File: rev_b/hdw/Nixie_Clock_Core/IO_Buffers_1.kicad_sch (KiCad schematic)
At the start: 14 parts, among them U2801 74VHC541, U2802 74VHC541, U2803 74LVC1G97, U2804 74LVC1G97

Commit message: lots of rev B control board schematic progress
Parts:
- removed C? (x2): 0.1uF, Capacitors_SMD:C_0603, symbol Custom_Library:C_Custom
- removed R? (x2): 10K, Resistors_SMD:R_0603, symbol Custom_Library:R_Custom
- removed U2803, U2804: 74LVC1G97, Package_TO_SOT_SMD:SOT-363_SC-70-6, symbol Custom_Library:74LVC1G97_Power_BUF
- renumbered RN2801 to RN?, RN2802 to RN?, U2801 to U?, U2802 to U?
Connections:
- net +5V is gone; now on net +3.3V: C?.1, C?.1, U?.20 (VCC), U?.20 (VCC)
- net Grid_2 is gone; now on net Anode_DP: RN?.14 (R3.2), U?.4 (A2)
- net Grid_3 is gone; now on net Colon_0: RN?.13 (R4.2), U?.5 (A3)
- net Grid_4 is gone; now on net Colon_1: RN?.12 (R5.2), U?.6 (A4)
- net Grid_5 is gone; now on net Colon_2: RN?.11 (R6.2), U?.7 (A5)
- net Anode_DP: no longer RN?.9 (R8.2), U?.9 (A7)
- net Colon_0: no longer RN?.10 (R7.2), U?.8 (A6)
- net Colon_1: no longer RN?.9 (R8.2), U?.9 (A7)
- net Colon_3: now also RN?.10 (R7.2), U?.8 (A6)
- net Anode_A renamed Anode_0
- net Anode_A_DSP: no longer names the net of U?.18 (Y0)
- net Anode_B renamed Anode_1
- net Anode_B_DSP: no longer names the net of U?.17 (Y1)
- net Anode_C renamed Anode_2
- net Anode_C_DSP: no longer names the net of U?.16 (Y2)
- net Anode_D renamed Anode_3
- net Anode_DP_DSP: no longer names the net of U?.11 (Y7)
- net Anode_D_DSP: no longer names the net of U?.15 (Y3)
- net Anode_E renamed Anode_4
- net Anode_E_DSP: no longer names the net of U?.14 (Y4)
- net Anode_F renamed Anode_5
- net Anode_F_DSP: no longer names the net of U?.13 (Y5)
- net Anode_G renamed Anode_6
- net Anode_G_DSP: no longer names the net of U?.12 (Y6)
- net Colon_0_DSP: no longer names the net of U?.12 (Y6)
- net Colon_1_DSP: no longer names the net of U?.11 (Y7)
- net Grid_0 renamed Anode_8
- net Grid_0_DSP: no longer names the net of U?.18 (Y0)
- net Grid_1 renamed Anode_9
- net Grid_1_DSP: no longer names the net of U?.17 (Y1)
- net Grid_2_DSP: no longer names the net of U?.16 (Y2)
- net Grid_3_DSP: no longer names the net of U?.15 (Y3)
- net Grid_4_DSP: no longer names the net of U?.14 (Y4)
- net Grid_5_DSP: no longer names the net of U?.13 (Y5)
- new net: RN?.9 (R8.2), U?.9 (A7)
- new net Anode_7: RN?.9 (R8.2), U?.9 (A7)

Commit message: more rev b sch progress
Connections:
- net Anode_7_DSP: now reaches U?.11 (Y7)
- net Anode_6_DSP: now reaches U?.12 (Y6)
- net Anode_5_DSP: now reaches U?.13 (Y5)
- net Anode_4_DSP: now reaches U?.14 (Y4)
- net Anode_3_DSP: now reaches U?.15 (Y3)
- net Anode_2_DSP: now reaches U?.16 (Y2)
- net Anode_1_DSP: now reaches U?.17 (Y1)
- net Anode_0_DSP: now reaches U?.18 (Y0)
- net Colon_3_DSP: now reaches U?.12 (Y6)
- net Colon_2_DSP: now reaches U?.13 (Y5)
- net Colon_1_DSP: now reaches U?.14 (Y4)
- net Colon_0_DSP: now reaches U?.15 (Y3)
- net Anode_DP_DSP: now reaches U?.16 (Y2)
- net Anode_9_DSP: now reaches U?.17 (Y1)
- net Anode_8_DSP: now reaches U?.18 (Y0)
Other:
- moved on the sheet: RN?, U?

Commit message: more carrier board progress
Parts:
- removed C?: 0.1uF, Capacitors_SMD:C_0603, symbol Custom_Library:C_Custom
- removed R?: 10K, Resistors_SMD:R_0603, symbol Custom_Library:R_Custom
- removed RN?: 10k, Resistors_SMD:R_Array_Convex_8x0602, symbol Device:R_Pack08
- removed U?: 74VHC541, Package_DFN_QFN:WQFN-20-1EP_2.5x4.5mm_P0.5mm_EP1x2.9mm, symbol Custom_Library:74VHC541
- added C? (x2): 0.1uF, Capacitors_SMD:C_0603, symbol Custom_Library:C_Custom
- added R? (x2): 10K, Resistors_SMD:R_0603, symbol Custom_Library:R_Custom
- added RN? (x2): 10k, Resistors_SMD:R_Array_Convex_8x0602, symbol Device:R_Pack08
- added U? (x2): 74VHC541, Package_DFN_QFN:WQFN-20-1EP_2.5x4.5mm_P0.5mm_EP1x2.9mm, symbol Custom_Library:74VHC541
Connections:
- net +3.3V: now also C?.1, C?.1, R?.1, R?.1, U?.20 (VCC), U?.20 (VCC)
- net Colon_0: now also RN?.13 (R4.2), U?.5 (A3)
- net Colon_0_DSP: now also U?.15 (Y3)
- net Colon_1: now also RN?.12 (R5.2), U?.6 (A4)
- net Colon_1_DSP: now also U?.14 (Y4)
- net Colon_2: now also RN?.11 (R6.2), U?.7 (A5)
- net Colon_2_DSP: now also U?.13 (Y5)
- net Colon_3: now also RN?.10 (R7.2), U?.8 (A6)
- net Colon_3_DSP: now also U?.12 (Y6)
- net GND: now also C?.2, C?.2, RN?.1 (R1.1), RN?.1 (R1.1), RN?.2 (R2.1), RN?.2 (R2.1), RN?.3 (R3.1), RN?.3 (R3.1), RN?.4 (R4.1), RN?.4 (R4.1), RN?.5 (R5.1), RN?.5 (R5.1), RN?.6 (R6.1), RN?.6 (R6.1), RN?.7 (R7.1), RN?.7 (R7.1), RN?.8 (R8.1), RN?.8 (R8.1), U?.10 (GND), U?.10 (GND), U?.21 (GND), U?.21 (GND)
- net ~{IO_Level_Shift_Enable}: now also R?.2, R?.2, U?.1 (G1), U?.1 (G1), U?.19 (G2), U?.19 (G2)
- net Anode_6: no longer names the net of RN?.10 (R7.2), U?.8 (A6)
- net Anode_6_DSP: no longer names the net of U?.12 (Y6)
- net Anode_7: no longer names the net of RN?.9 (R8.2), U?.9 (A7)
- net Anode_7_DSP: no longer names the net of U?.11 (Y7)
- new net: RN?.9 (R8.2), U?.9 (A7)
- new net Cathode_0: RN?.16 (R1.2), U?.2 (A0)
- new net Cathode_0_DSP: U?.18 (Y0)
- new net Cathode_1: RN?.15 (R2.2), U?.3 (A1)
- new net Cathode_1_DSP: U?.17 (Y1)
- new net Cathode_2: RN?.14 (R3.2), U?.4 (A2)
- new net Cathode_2_DSP: U?.16 (Y2)
- new net Cathode_3: RN?.13 (R4.2), U?.5 (A3)
- new net Cathode_3_DSP: U?.15 (Y3)
- new net Cathode_4: RN?.12 (R5.2), U?.6 (A4)
- new net Cathode_4_DSP: U?.14 (Y4)
- new net Cathode_5: RN?.11 (R6.2), U?.7 (A5)
- new net Cathode_5_DSP: U?.13 (Y5)
- new net Cathode_6: RN?.10 (R7.2), U?.8 (A6)
- new net Cathode_6_DSP: U?.12 (Y6)
- new net Cathode_7: RN?.9 (R8.2), U?.9 (A7)
- new net Cathode_7_DSP: U?.11 (Y7)
- new net Cathode_8: RN?.16 (R1.2), U?.2 (A0)
- new net Cathode_8_DSP: U?.18 (Y0)
- new net Cathode_9: RN?.15 (R2.2), U?.3 (A1)
- new net Cathode_9_DSP: U?.17 (Y1)
- new net Cathode_DP: RN?.14 (R3.2), U?.4 (A2)
- new net Cathode_DP_DSP: U?.16 (Y2)
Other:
- note removed: "CONSIDER SINGLE RESISTORS INSTEAD OF RPACKS"
- moved on the sheet: C?, R?, RN?, U?

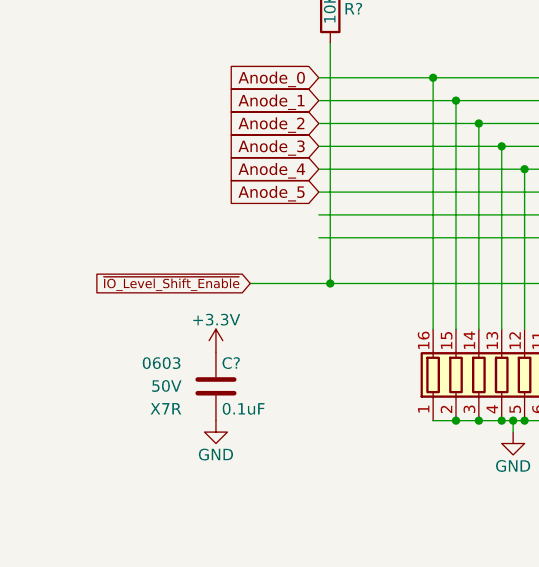
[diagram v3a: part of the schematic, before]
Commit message: more schematic progress, assigning signals to MCU"
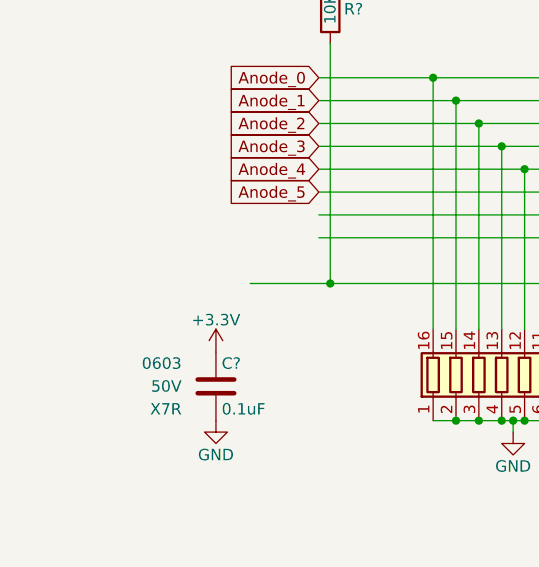
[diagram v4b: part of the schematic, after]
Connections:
- net ~{IO_Level_Shift_Enable}: no longer R?.2, U?.1 (G1), U?.19 (G2)
- new net: R?.2, U?.1 (G1), U?.19 (G2)
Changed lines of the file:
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@@
-    )
-  )
-  (global_label "~{IO_Level_Shift_Enable}" (shape input) (at 36.83 58.42 180)
-    (effects (font (size 1.016 1.016)) (justify right))
-    (property "Intersheetrefs" "${INTERSHEET_REFS}" (at 36.83 58.42 0)
-      (effects (font (size 1.27 1.27)) hide)
     )
   )

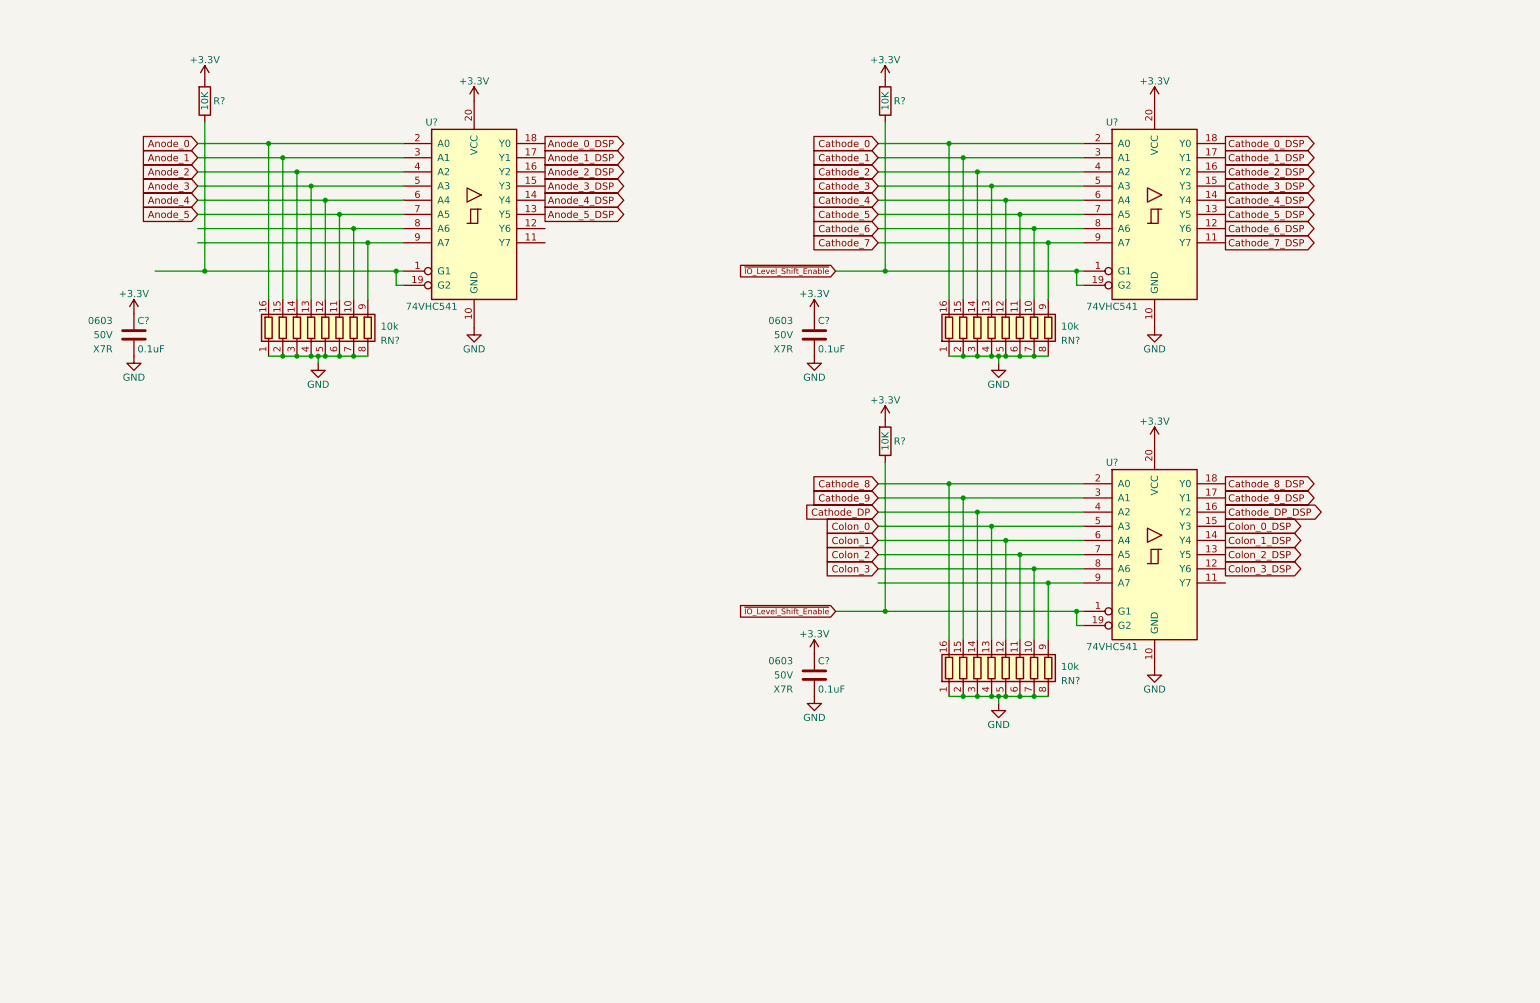
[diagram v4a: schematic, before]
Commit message: updated footprints, ran some DRC
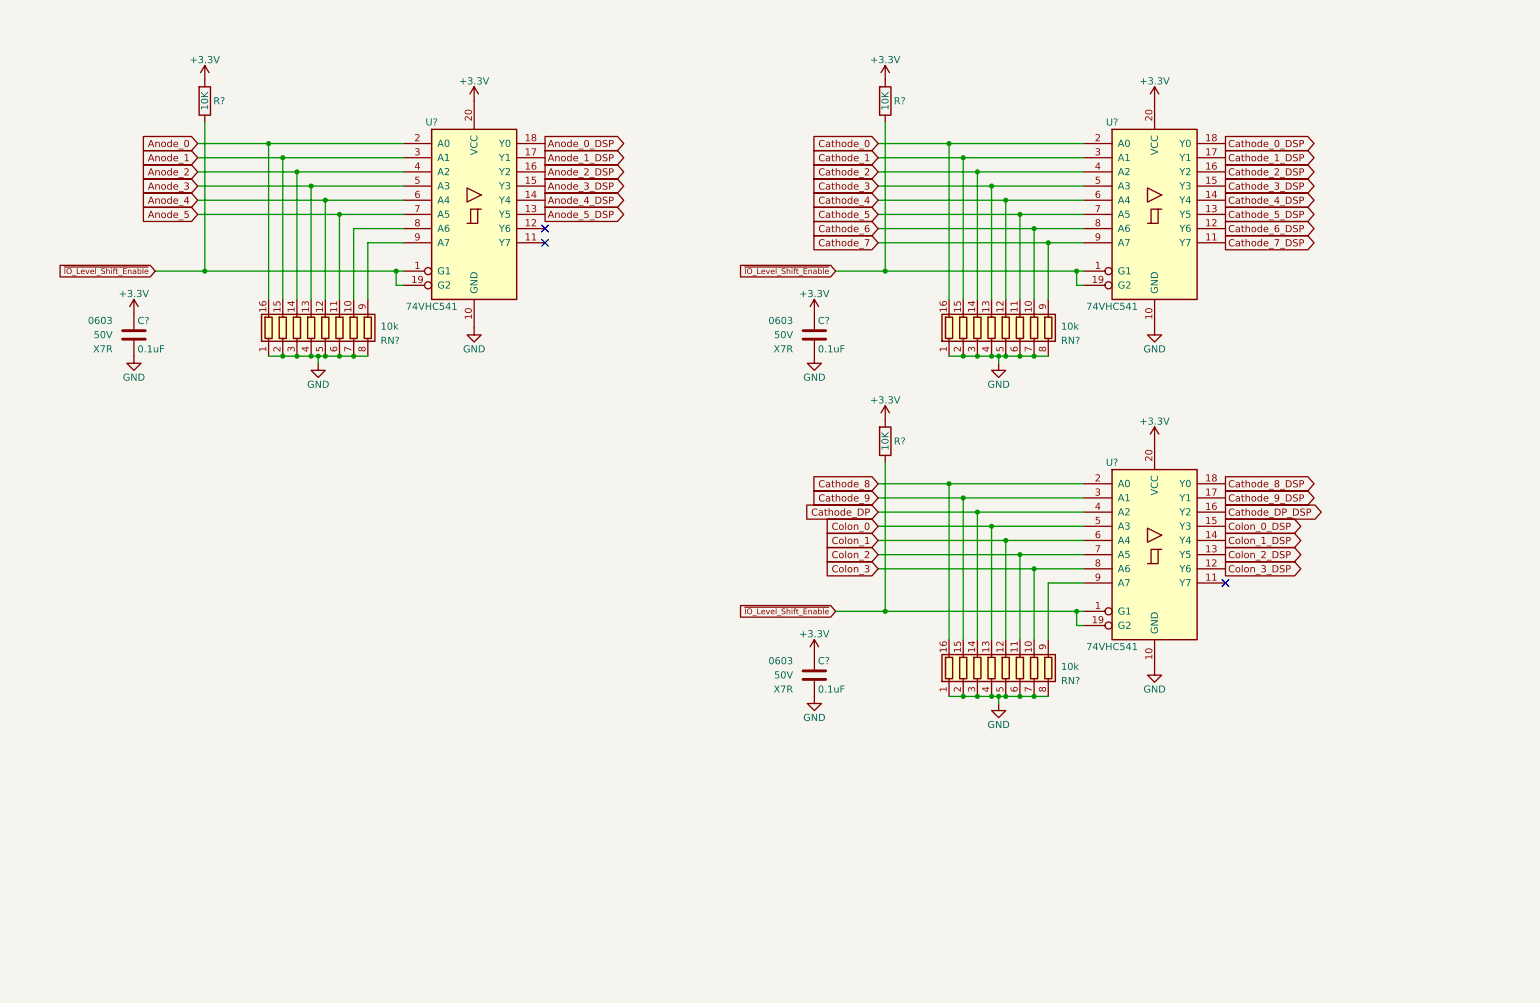
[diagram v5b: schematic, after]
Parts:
- C? (x3): Digi-Key PN 311-1344-1-ND -> (none)
- R? (x3): Digi-Key PN RHM10KADCT-ND -> (none)
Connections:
- net ~{IO_Level_Shift_Enable}: now also R?.2, U?.1 (G1), U?.19 (G2)
- no-connect marks 0 -> 3
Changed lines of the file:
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@@
   (junction (at 67.31 45.72) (diameter 0) (color 0 0 0 0)
   )
-  (junction (at 74.93 53.34) (diameter 0) (color 0 0 0 0)
-  )
   (junction (at 69.85 73.66) (diameter 0) (color 0 0 0 0)
   )
@@
   (junction (at 189.23 134.62) (diameter 0) (color 0 0 0 0)
   )
-  (junction (at 196.85 114.3) (diameter 0) (color 0 0 0 0)
-  )
   (junction (at 184.15 101.6) (diameter 0) (color 0 0 0 0)
   )
@@
   (junction (at 184.15 73.66) (diameter 0) (color 0 0 0 0)
   )
-  (junction (at 72.39 50.8) (diameter 0) (color 0 0 0 0)
-  )
   (junction (at 191.77 134.62) (diameter 0) (color 0 0 0 0)
   )
@@
   (junction (at 196.85 53.34) (diameter 0) (color 0 0 0 0)
   )
+  (no_connect (at 106.68 50.8))
+  (no_connect (at 106.68 53.34))
+  (no_connect (at 228.6 114.3))
   (wire (pts (xy 191.77 73.66) (xy 194.31 73.66))
     (stroke (width 0) (type default))
@@
     (stroke (width 0) (type default))
   )
-  (wire (pts (xy 44.45 50.8) (xy 72.39 50.8))
-    (stroke (width 0) (type default))
-  )
   (wire (pts (xy 167.64 119.38) (xy 167.64 92.71))
     (stroke (width 0) (type default))
@@
     (stroke (width 0) (type default))
   )
-  (wire (pts (xy 166.37 114.3) (xy 196.85 114.3))
-    (stroke (width 0) (type default))
-  )
   (wire (pts (xy 69.85 73.66) (xy 72.39 73.66))
     (stroke (width 0) (type default))
@@
   )
   (wire (pts (xy 80.01 60.96) (xy 80.01 58.42))
-    (stroke (width 0) (type default))
-  )
-  (wire (pts (xy 44.45 53.34) (xy 74.93 53.34))
     (stroke (width 0) (type default))
   )
@@
     (property "Intersheetrefs" "${INTERSHEET_REFS}" (at 246.0803 53.34 0)
       (effects (font (size 1.27 1.27)) (justify left) hide)
+    )
+  )
+  (global_label "~{IO_Level_Shift_Enable}" (shape input) (at 36.83 58.42 180)
+    (effects (font (size 1.016 1.016)) (justify right))
+    (property "Intersheetrefs" "${INTERSHEET_REFS}" (at 36.83 58.42 0)
+      (effects (font (size 1.27 1.27)) hide)
     )
   )
@@
       (project "Nixie_Clock_Core"
         (path "/16fdce21-b570-4d81-a458-e8839d611806/010acd62-4c34-490e-a56e-313765aa4851"
-          (reference "RN?") (unit 1)
+          (reference "RN1701") (unit 1)
         )
       )
@@
       (project "Nixie_Clock_Core"
         (path "/16fdce21-b570-4d81-a458-e8839d611806/010acd62-4c34-490e-a56e-313765aa4851"
-          (reference "RN?") (unit 1)
+          (reference "RN1703") (unit 1)
         )
       )
@@
       (project "Nixie_Clock_Core"
         (path "/16fdce21-b570-4d81-a458-e8839d611806/010acd62-4c34-490e-a56e-313765aa4851"
-          (reference "RN?") (unit 1)
+          (reference "RN1702") (unit 1)
         )
       )
@@
       (effects (font (size 1.27 1.27)) (justify left) hide)
     )
-    (property "Digi-Key PN" "RHM10KADCT-ND" (at 160.02 17.78 0)
+    (property "Digi-Key PN" "" (at 160.02 17.78 0)
       (effects (font (size 1.524 1.524)) hide)
     )
@@
       (project "Nixie_Clock_Core"
         (path "/16fdce21-b570-4d81-a458-e8839d611806/010acd62-4c34-490e-a56e-313765aa4851"
-          (reference "R?") (unit 1)
+          (reference "R1702") (unit 1)
         )
       )
@@
       (project "Nixie_Clock_Core"
         (path "/16fdce21-b570-4d81-a458-e8839d611806/010acd62-4c34-490e-a56e-313765aa4851"
-          (reference "U?") (unit 1)
+          (reference "U1703") (unit 1)
         )
       )
@@
       (project "Nixie_Clock_Core"
         (path "/16fdce21-b570-4d81-a458-e8839d611806/010acd62-4c34-490e-a56e-313765aa4851"
-          (reference "U?") (unit 1)
+          (reference "U1702") (unit 1)
         )
       )
@@
       (project "Nixie_Clock_Core"
         (path "/16fdce21-b570-4d81-a458-e8839d611806/010acd62-4c34-490e-a56e-313765aa4851"
-          (reference "#PWR?") (unit 1)
+          (reference "#PWR01704") (unit 1)
         )
       )
@@
       (project "Nixie_Clock_Core"
         (path "/16fdce21-b570-4d81-a458-e8839d611806/010acd62-4c34-490e-a56e-313765aa4851"
-          (reference "U?") (unit 1)
+          (reference "U1701") (unit 1)
         )
       )
@@
       (effects (font (size 1.27 1.27)) (justify right))
     )
-    (property "Digi-Key PN" "311-1344-1-ND" (at 165.735 118.11 0)
+    (property "Digi-Key PN" "" (at 165.735 118.11 0)
       (effects (font (size 1.524 1.524)) hide)
     )
@@
       (project "Nixie_Clock_Core"
         (path "/16fdce21-b570-4d81-a458-e8839d611806/010acd62-4c34-490e-a56e-313765aa4851"
-          (reference "C?") (unit 1)
+          (reference "C1703") (unit 1)
         )
       )
@@
       (effects (font (size 1.27 1.27)) (justify right))
     )
-    (property "Digi-Key PN" "311-1344-1-ND" (at 43.815 57.15 0)
+    (property "Digi-Key PN" "" (at 43.815 57.15 0)
       (effects (font (size 1.524 1.524)) hide)
     )
@@
       (project "Nixie_Clock_Core"
         (path "/16fdce21-b570-4d81-a458-e8839d611806/010acd62-4c34-490e-a56e-313765aa4851"
-          (reference "C?") (unit 1)
+          (reference "C1701") (unit 1)
         )
       )
@@
       (effects (font (size 1.27 1.27)) (justify right))
     )
-    (property "Digi-Key PN" "311-1344-1-ND" (at 165.735 57.15 0)
+    (property "Digi-Key PN" "" (at 165.735 57.15 0)
       (effects (font (size 1.524 1.524)) hide)
     )
@@
       (project "Nixie_Clock_Core"
         (path "/16fdce21-b570-4d81-a458-e8839d611806/010acd62-4c34-490e-a56e-313765aa4851"
-          (reference "C?") (unit 1)
+          (reference "C1702") (unit 1)
         )
       )
@@
       (project "Nixie_Clock_Core"
         (path "/16fdce21-b570-4d81-a458-e8839d611806/010acd62-4c34-490e-a56e-313765aa4851"
-          (reference "#PWR?") (unit 1)
+          (reference "#PWR01703") (unit 1)
         )
       )
@@
       (project "Nixie_Clock_Core"
         (path "/16fdce21-b570-4d81-a458-e8839d611806/010acd62-4c34-490e-a56e-313765aa4851"
-          (reference "#PWR?") (unit 1)
+          (reference "#PWR01717") (unit 1)
         )
       )
@@
       (effects (font (size 1.27 1.27)) (justify left) hide)
     )
-    (property "Digi-Key PN" "RHM10KADCT-ND" (at 38.1 17.78 0)
+    (property "Digi-Key PN" "" (at 38.1 17.78 0)
       (effects (font (size 1.524 1.524)) hide)
     )
@@
       (project "Nixie_Clock_Core"
         (path "/16fdce21-b570-4d81-a458-e8839d611806/010acd62-4c34-490e-a56e-313765aa4851"
-          (reference "R?") (unit 1)
+          (reference "R1701") (unit 1)
         )
       )
@@
       (effects (font (size 1.27 1.27)) (justify left) hide)
     )
-    (property "Digi-Key PN" "RHM10KADCT-ND" (at 160.02 78.74 0)
+    (property "Digi-Key PN" "" (at 160.02 78.74 0)
       (effects (font (size 1.524 1.524)) hide)
     )
@@
       (project "Nixie_Clock_Core"
         (path "/16fdce21-b570-4d81-a458-e8839d611806/010acd62-4c34-490e-a56e-313765aa4851"
-          (reference "R?") (unit 1)
+          (reference "R1703") (unit 1)
         )
       )
@@
       (project "Nixie_Clock_Core"
         (path "/16fdce21-b570-4d81-a458-e8839d611806/010acd62-4c34-490e-a56e-313765aa4851"
-          (reference "#PWR?") (unit 1)
-        )
-      )
+          (reference "#PWR01718") (unit 1)
+        )
+      )

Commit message: hid all passive refdes on core PCB
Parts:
- C? (x3): Digi-Key PN (none) -> 1276-1935-1-ND
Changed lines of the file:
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@@
       (effects (font (size 1.27 1.27)) (justify right))
     )
-    (property "Digi-Key PN" "" (at 165.735 118.11 0)
+    (property "Digi-Key PN" "1276-1935-1-ND" (at 165.735 118.11 0)
       (effects (font (size 1.524 1.524)) hide)
     )
@@
       (effects (font (size 1.27 1.27)) (justify right))
     )
-    (property "Digi-Key PN" "" (at 43.815 57.15 0)
+    (property "Digi-Key PN" "1276-1935-1-ND" (at 43.815 57.15 0)
       (effects (font (size 1.524 1.524)) hide)
     )
@@
       (effects (font (size 1.27 1.27)) (justify right))
     )
-    (property "Digi-Key PN" "" (at 165.735 57.15 0)
+    (property "Digi-Key PN" "1276-1935-1-ND" (at 165.735 57.15 0)
       (effects (font (size 1.524 1.524)) hide)
     )

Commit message: added BOM
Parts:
- R? (x3): Digi-Key PN (none) -> 541-10.0KHCT-ND
- RN? (x3): Tolerance (none) -> 1%
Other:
- title: (none) -> Nixie Clock Redux Core Board
